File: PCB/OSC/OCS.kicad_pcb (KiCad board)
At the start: 2 copper layers, 70 x 70 mm, 47 parts, among them J1 Reset, J2 Wago, J3 TC2030-USB-NL-DS, J4 SPK, J5 USB-C-Socket-H, J6 RELAY, SW1 Button, U1 ICS43434_MEMS_Mic, U2 MAX98357A, U3 Relay, U4 78L05, U5 IRM-H638T/TR2, U6 ESP32-S3-MINI-1, U7 MD8942

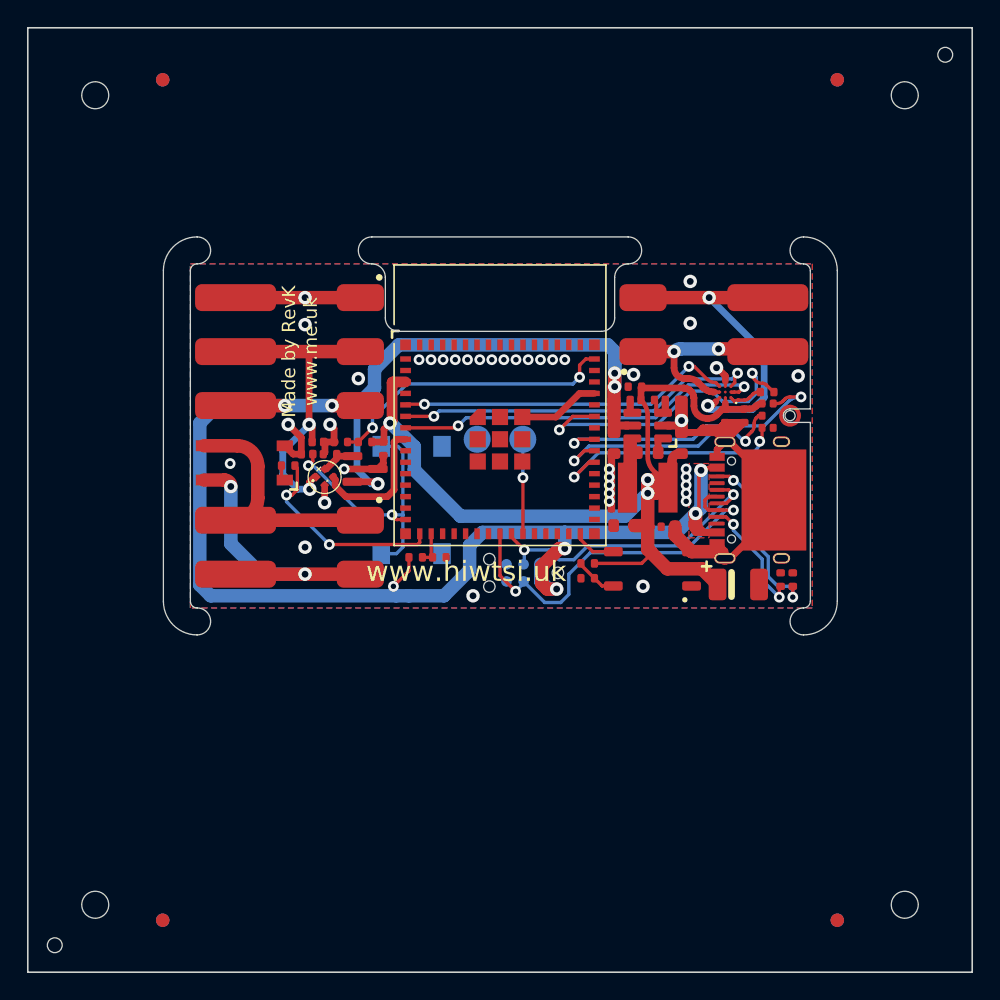
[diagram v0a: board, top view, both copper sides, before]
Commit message: Getting basic BOM
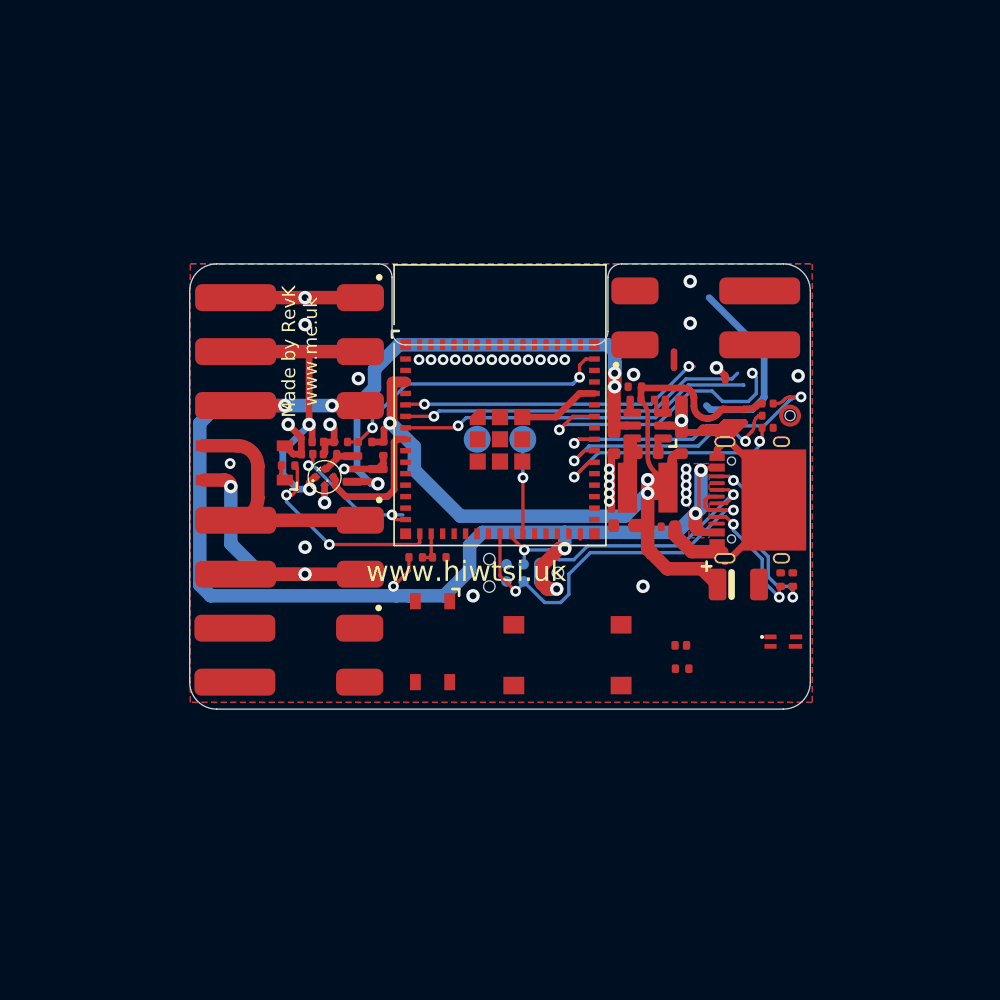
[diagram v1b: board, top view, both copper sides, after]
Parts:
- removed C13: 10uF, RevK:C_0402
- removed C14: 100nF, RevK:C_0402
- removed C4: 4.7uF, RevK:C_0402
- removed PCB1: 70x70, RevK:PCB7070
- removed R8: 634K, RevK:R_0402
- removed R9: 100R, RevK:R_0402
- removed U2: MAX98357A, RevK:WLP-1.437mmx1.347mm-0.21mm-ball
- removed U5: IRM-H638T/TR2, RevK:SMD-4P,4x5mm
- removed V1, V2: ~, RevK:VCUT70N
- added D5: ~, RevK:DFN1006-2L, F.Cu at (113.4, 110.8)
- added J7: RELAY2, RevK:WAGO-2060-452-998-404, F.Cu at (85.0, 111.5)
- added R10: 1K, RevK:R_0402, F.Cu at (113.5, 112.5)
- added U8: Relay, RevK:SO-4_4.4x4.3mm_P2.54mm, F.Cu at (95.0, 110.5)
- added U9: VEML6040, RevK:VEML6040, F.Cu at (121.0, 110.5)
- J4: value SPK -> DC
- J6: value RELAY -> RELAY1
- SW1: moved to F.Cu
- moved SW1 16.3 mm to (105.0, 111.5), turned to 0 degrees
- moved J4 0.78 mm to (114.6, 86.5)
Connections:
- net RELAY renamed RELAY1
- J4 pad 1: Net-(J4-Pin_1) -> GND
- J4 pad 2: Net-(J4-Pin_2) -> DC
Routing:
- net Net-(J4-Pin_2): track 23.8 -> 0.00 mm, vias 2 -> 0
- net (no net): track 0.00 -> 15.1 mm
- net Net-(J4-Pin_1): track 14.0 -> 0.00 mm, vias 2 -> 0
- net PUSH: track 21.3 -> 10.6 mm
- net +3V3: track 65.8 -> 60.8 mm
- net Net-(U5-VCC): track 3.05 -> 0.00 mm
- net IR: track 3.24 -> 0.40 mm
- net SKPPWR: track 23.2 -> 21.0 mm
- net Net-(U2-~{SD_MODE}): track 2.13 -> 0.00 mm
- net SKPWS: track 24.6 -> 22.5 mm
- net SKPSD: track 27.3 -> 26.4 mm, vias 2 -> 1
- net SKPSCK: track 26.7 -> 25.9 mm, vias 2 -> 1
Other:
- board size 70 x 70 mm -> 46 x 33 mm
